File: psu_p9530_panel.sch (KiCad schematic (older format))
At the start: 58 parts, among them IC306 LTC1658, IC308 CD4052B, IC310 TLC272, IC312 TLC272, U401 54LS164

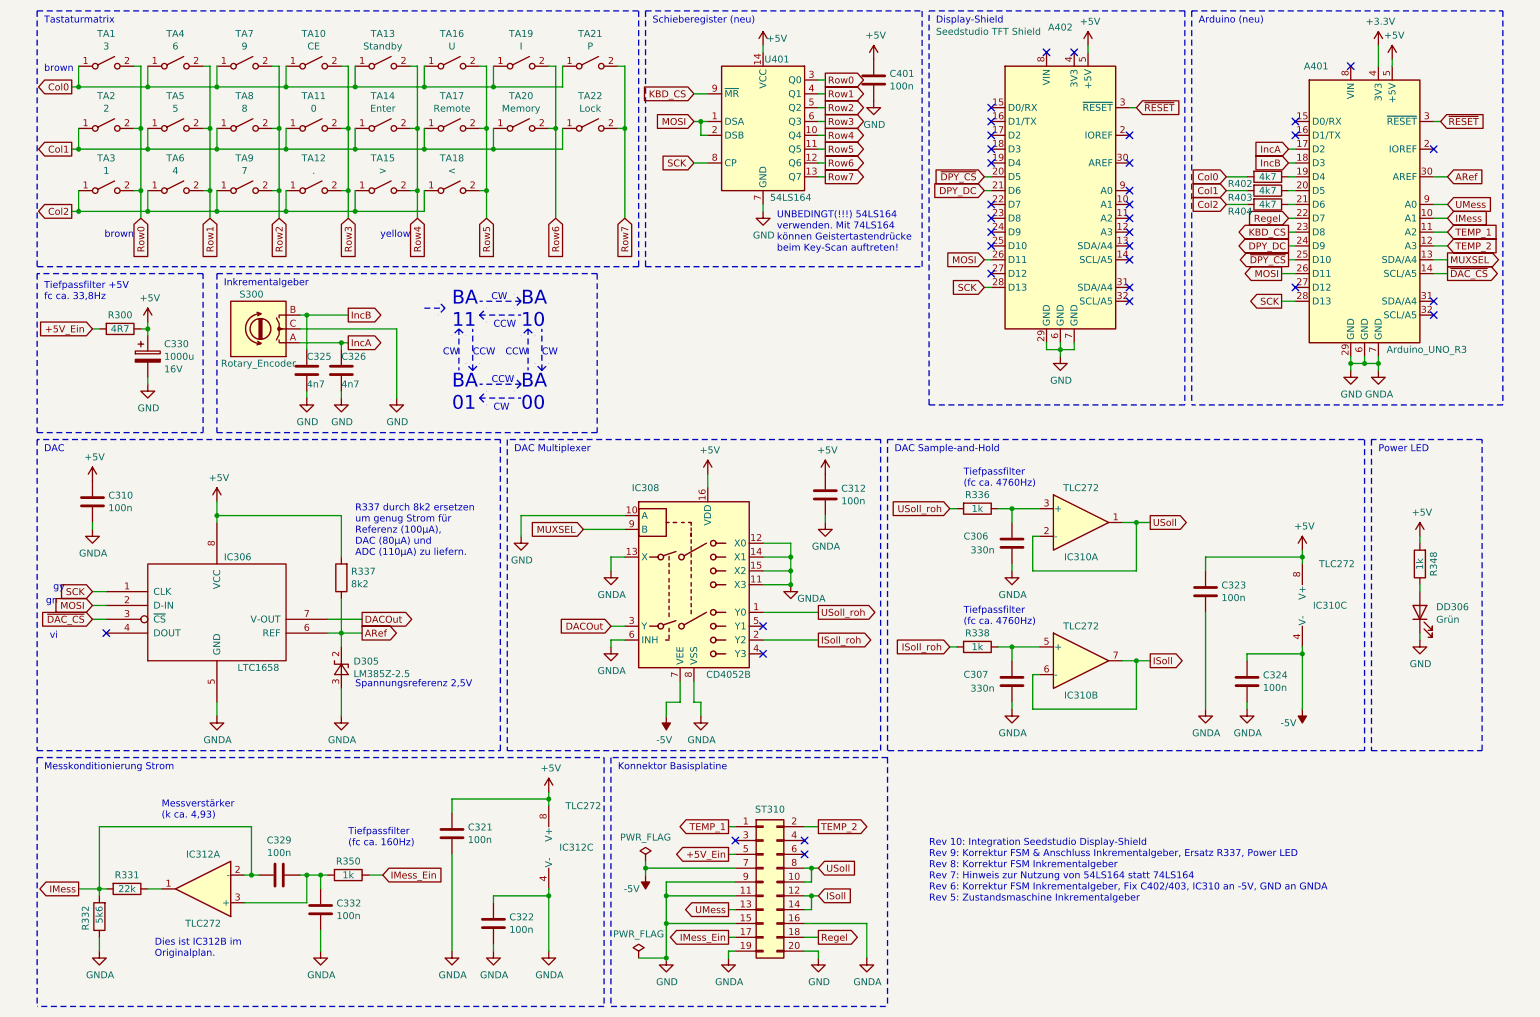
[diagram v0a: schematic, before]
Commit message: Introduce measurement and conversion of temperature data
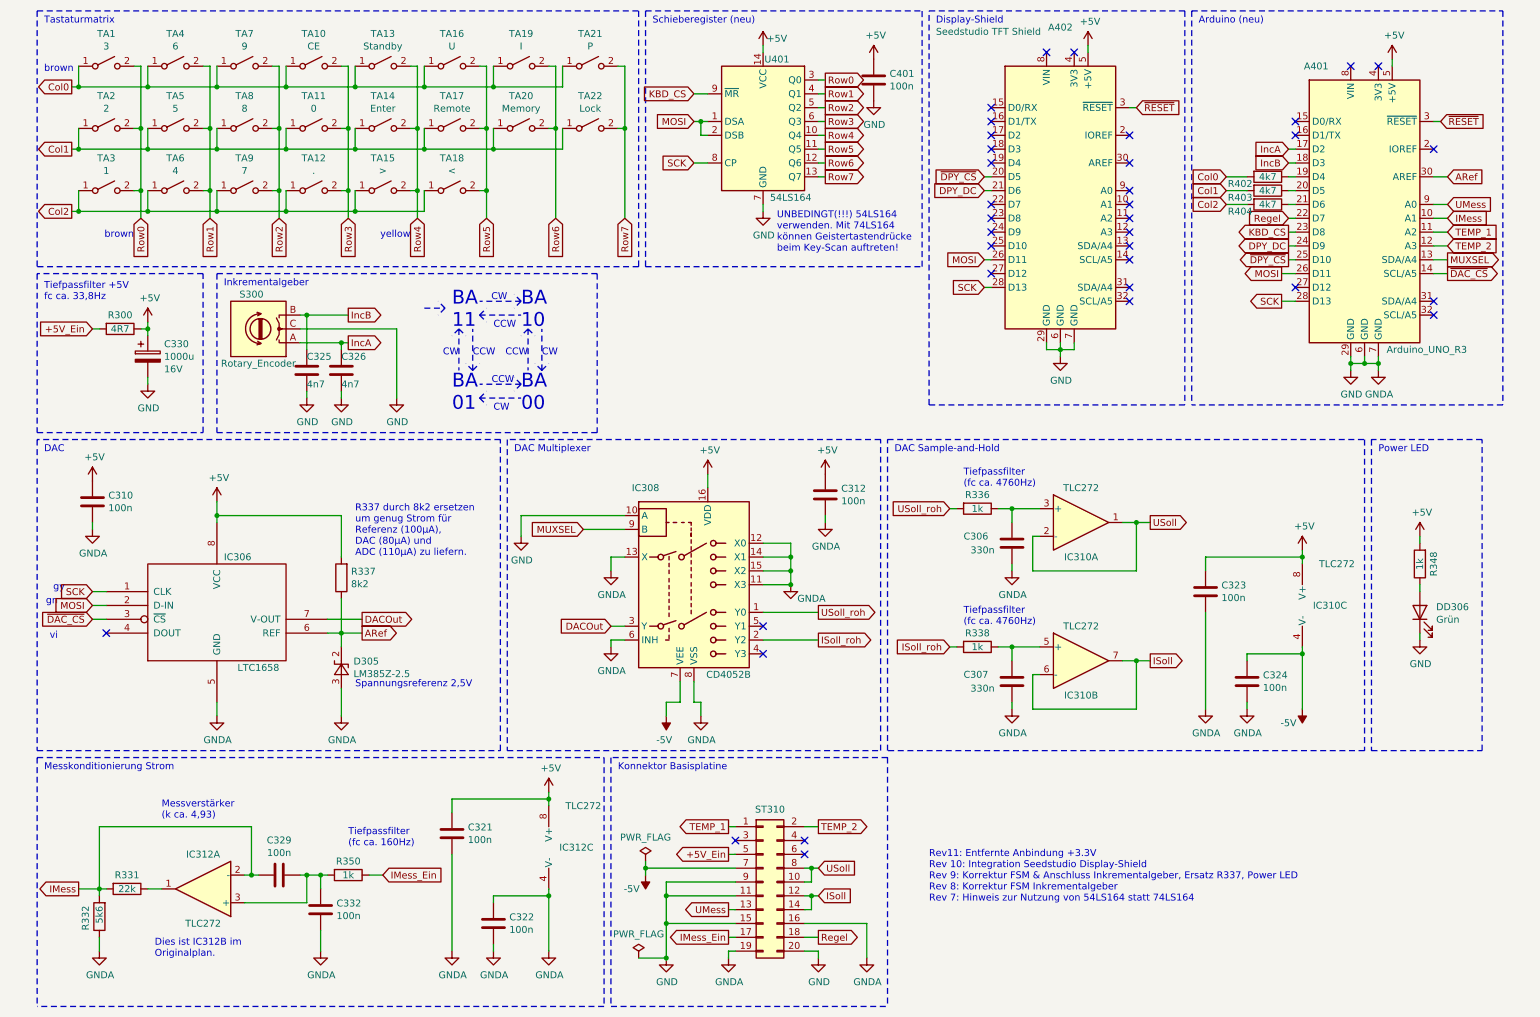
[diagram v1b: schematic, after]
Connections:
- net +3V3: no longer names the net of A401.4 (3V3)
- no-connect marks 35 -> 36
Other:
- note added: "Rev11: Entfernte Anbindung +3.3V\nRev 10: Integration Seedstudio Display-Shield\nRev 9: Korrektur FSM & Anschluss Inkrementalgeber, Ersatz R337, Power LED\nRev 8: Korrektur FSM Inkrementalgeber\nRev 7: Hinweis zur Nutzung von 54LS164 statt 74LS164"
- note removed: "Rev 10: Integration Seedstudio Display-Shield\nRev 9: Korrektur FSM & Anschluss Inkrementalgeber, Ersatz R337, Power LED\nRev 8: Korrektur FSM Inkrementalgeber\nRev 7: Hinweis zur Nutzung von 54LS164 statt 74LS164\nRev 6: Korrektur FSM Inkrementalgeber, Fix C402/403, IC310 an -5V, GND an GNDA\nRev 5: Zustandsmaschine Inkrementalgeber"
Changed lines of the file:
@@
 	1750 3600 1750 2450
 Text Notes 7000 7000 0    50   ~ 0
-Rev 10: Integration Seedstudio Display-Shield\nRev 9: Korrektur FSM & Anschluss Inkrementalgeber, Ersatz R337, Power LED\nRev 8: Korrektur FSM Inkrementalgeber\nRev 7: Hinweis zur Nutzung von 54LS164 statt 74LS164\nRev 6: Korrektur FSM Inkrementalgeber, Fix C402/403, IC310 an -5V, GND an GNDA\nRev 5: Zustandsmaschine Inkrementalgeber
+Rev11: Entfernte Anbindung +3.3V\nRev 10: Integration Seedstudio Display-Shield\nRev 9: Korrektur FSM & Anschluss Inkrementalgeber, Ersatz R337, Power LED\nRev 8: Korrektur FSM Inkrementalgeber\nRev 7: Hinweis zur Nutzung von 54LS164 statt 74LS164
 $Comp
 L Device:R R402
@@
 Wire Wire Line
 	9150 1950 9300 1950
-$Comp
-L power:+3.3V #PWR0415
-U 1 1 63267B2E
-P 10250 800
-F 0 "#PWR0415" H 10250 650 50  0001 C CNN
-F 1 "+3.3V" H 10265 973 50  0000 C CNN
-F 2 "" H 10250 800 50  0001 C CNN
-F 3 "" H 10250 800 50  0001 C CNN
-	1    10250 800
-	1    0    0    -1
-$EndComp
-Wire Wire Line
-	10250 800  10250 950
 Wire Notes Line
 	8900 550  8900 3400
@@
 Wire Notes Line
 	4900 2400 550  2400
+NoConn ~ 10250 950
 $EndSCHEMATC

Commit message: Add filter capacitors for keyboard matrix to avoid cross-talk with encoder lines
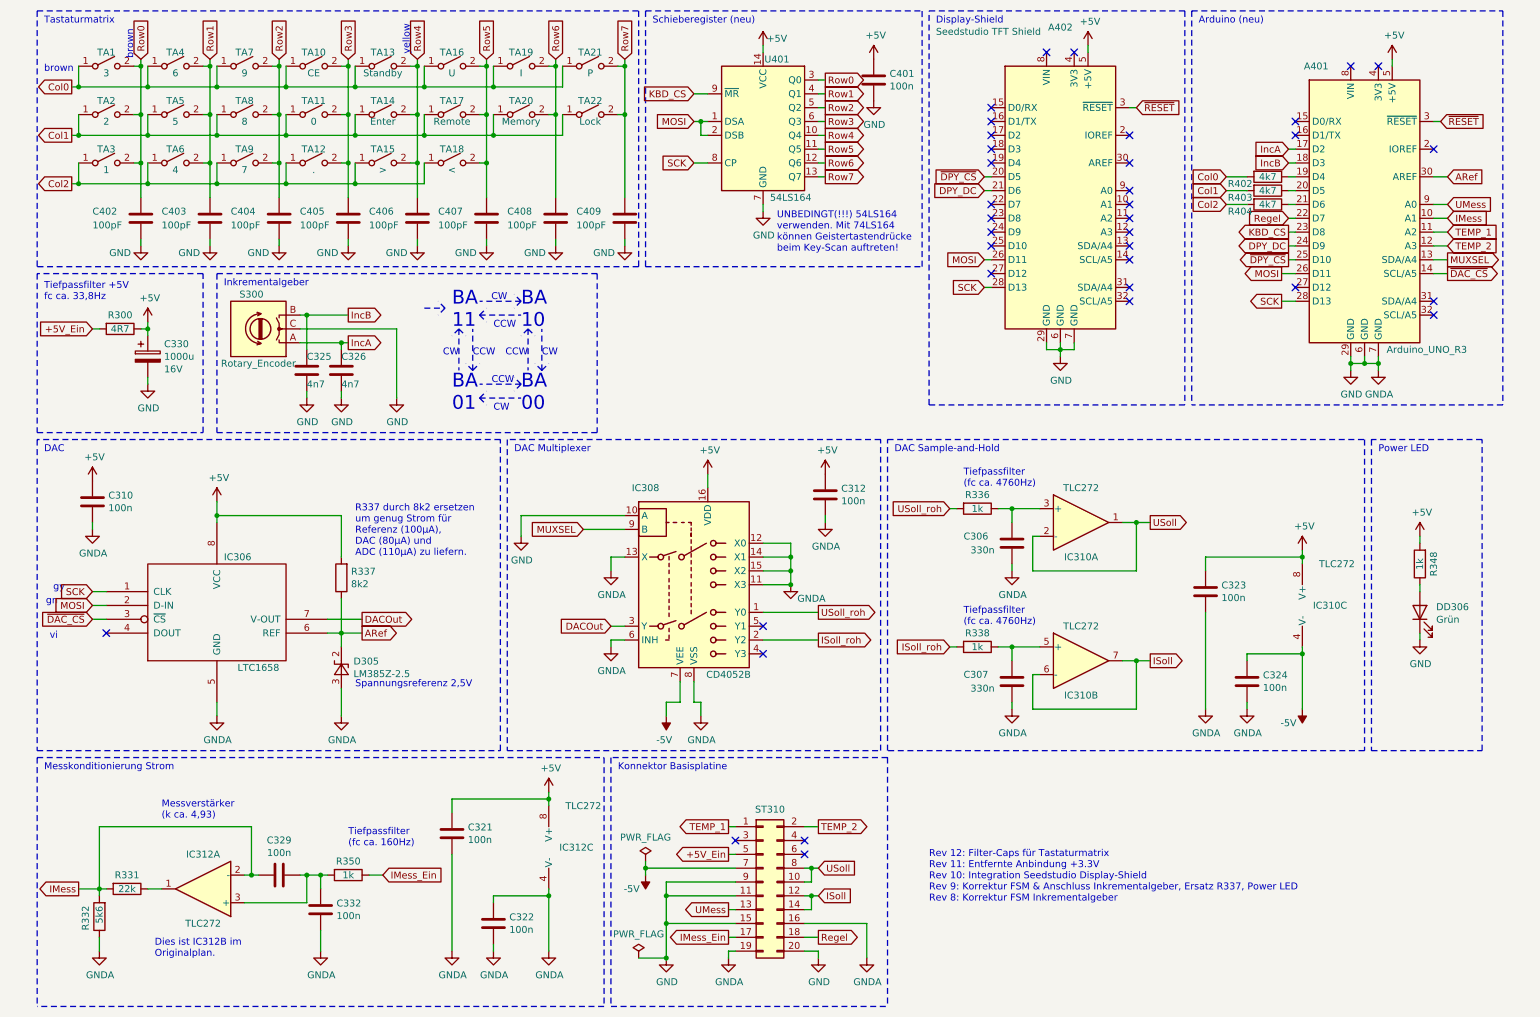
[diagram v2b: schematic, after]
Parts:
- added C402, C403, C404, C405, C406, C407, C408, C409: 100pF, symbol Device:C
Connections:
- net GND: now also C402.2, C403.2, C404.2, C405.2, C406.2, C407.2, C408.2, C409.2
- net Row0: now also C402.1
- net Row1: now also C403.1
- net Row2: now also C404.1
- net Row3: now also C405.1
- net Row4: now also C406.1
- net Row5: now also C407.1
- net Row6: now also C408.1
- net Row7: now also C409.1
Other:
- note added: "Rev 12: Filter-Caps für Tastaturmatrix\nRev 11: Entfernte Anbindung +3.3V\nRev 10: Integration Seedstudio Display-Shield\nRev 9: Korrektur FSM & Anschluss Inkrementalgeber, Ersatz R337, Power LED\nRev 8: Korrektur FSM Inkrementalgeber"
- note removed: "Rev11: Entfernte Anbindung +3.3V\nRev 10: Integration Seedstudio Display-Shield\nRev 9: Korrektur FSM & Anschluss Inkrementalgeber, Ersatz R337, Power LED\nRev 8: Korrektur FSM Inkrementalgeber\nRev 7: Hinweis zur Nutzung von 54LS164 statt 74LS164"
- moved on the sheet: TA11, TA12, TA14, TA15, TA17, TA18, TA2, TA20, TA22, TA3, TA5, TA6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
